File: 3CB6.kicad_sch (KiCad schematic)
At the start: 1 part, among them U1 EF83

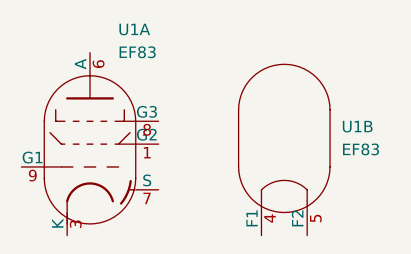
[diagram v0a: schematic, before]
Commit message: Modify EL83 symbol to 3CB6 pinout
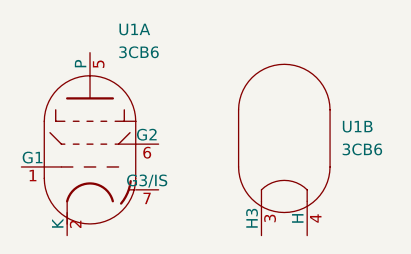
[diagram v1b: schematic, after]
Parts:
- U1: value EF83 -> 3CB6; symbol Valve:EF83 -> Valve:3CB6
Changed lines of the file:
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@@
 	(generator_version "9.0")
 	(paper "A4")
-	(symbol
-		(lib_id "Valve:EF83")
+       (symbol
+               (lib_id "Valve:3CB6")
 		(at 118.11 105.41 0)
 		(unit 1)
@@
 			)
 		)
-		(property "Value" "EF83"
+               (property "Value" "3CB6"
 			(at 121.2281 93.98 0)
 			(effects
@@
 			)
 		)
-		(pin "3"
-		)
-		(pin "9"
-		)
-		(pin "8"
-		)
-		(pin "6"
-		)
-		(pin "7"
-		)
-		(pin "1"
-		)
-		(pin "4"
-		)
-		(pin "5"
-		)
+               (pin "2"
+               )
+               (pin "1"
+               )
+               (pin "5"
+               )
+               (pin "7"
+               )
+               (pin "6"
+               )
+               (pin "3"
+               )
+               (pin "4"
+               )
 		(instances
 			(project ""
@@
 		)
 	)
-	(symbol
-		(lib_id "Valve:EF83")
+       (symbol
+               (lib_id "Valve:3CB6")
 		(at 139.7 104.14 0)
 		(unit 2)
@@
 			)
 		)
-		(property "Value" "EF83"
+               (property "Value" "3CB6"
 			(at 146.05 104.7749 0)
 			(effects
@@
 			)
 		)
-		(pin "3"
-		)
-		(pin "9"
-		)
-		(pin "8"
-		)
-		(pin "6"
-		)
-		(pin "7"
-		)
-		(pin "1"
-		)
-		(pin "4"
-		)
-		(pin "5"
-		)
+               (pin "2"
+               )
+               (pin "1"
+               )
+               (pin "5"
+               )
+               (pin "7"
+               )
+               (pin "6"
+               )
+               (pin "3"
+               )
+               (pin "4"
+               )
 		(instances
 			(project ""
